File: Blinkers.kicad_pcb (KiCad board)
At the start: 2 copper layers, 238 x 45 mm, 218 parts, among them J1 12V, J2 A1, J3 gnd, J4 A1, J5 A1, J6 A1, J7 A1, J8 A1, Q1 Q_NMOS_DGS, Q2 Q_NMOS_DGS, Q3 Q_NMOS_DGS, Q4 Q_NMOS_DGS, Q5 Q_NMOS_DGS, Q6 Q_NMOS_DGS

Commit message: Edge-cuts have been set to the Nova layout.
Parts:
- moved R30 22.5 mm to (242.3, 90.7)
- moved R31 22.5 mm to (242.3, 105.2)
- moved D10 22.5 mm to (38.6, 100.1)
- moved D104 22.5 mm to (149.5, 94.5)
- moved D105 22.5 mm to (149.5, 100.1)
- moved D108 22.5 mm to (149.5, 116.8)
- moved D114 22.5 mm to (161.8, 94.5)
- moved D115 22.5 mm to (161.8, 100.1)
- moved D118 22.5 mm to (161.8, 116.8)
- moved D122 22.5 mm to (174.1, 94.5)
- moved D123 22.5 mm to (174.1, 100.1)
- moved D126 22.5 mm to (174.1, 116.8)
- moved D13 22.5 mm to (38.6, 116.8)
- moved D131 22.5 mm to (186.4, 94.5)
- moved D132 22.5 mm to (186.4, 100.1)
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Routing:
- net 12V: track 673.9 -> 0.00 mm
- net GND: track 609.1 -> 0.00 mm
- net Net-(D1-Pad1): track 81.5 -> 0.00 mm
- net Net-(D10-Pad1): track 70.3 -> 0.00 mm
- net Net-(D36-Pad1): track 51.6 -> 0.00 mm
- net Net-(D105-Pad1): track 51.4 -> 0.00 mm
- net Net-(D63-Pad1): track 42.0 -> 0.00 mm
- net Net-(D123-Pad1): track 41.5 -> 0.00 mm
- net Net-(D150-Pad1): track 41.5 -> 0.00 mm
- net Net-(D25-Pad2): track 17.7 -> 0.00 mm
- net Net-(D22-Pad2): track 13.6 -> 0.00 mm
- net Net-(D91-Pad2): track 12.5 -> 0.00 mm
- net Net-(D78-Pad1): track 10.0 -> 0.00 mm
- net Net-(D77-Pad1): track 10.0 -> 0.00 mm
- net Net-(D165-Pad1): track 10.0 -> 0.00 mm
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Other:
- board size 238 x 45 mm -> 250 x 49 mm

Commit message: Main array x-axis positions and top row x-axis positions close to finished, WIP.
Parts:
- removed D10, D103, D104, D105, D106, D107, D108, D11, D113, D114, D115, D116, D117, D118, D12, D121, D122, D123, D124, D125, D126, D13, D130, D131, D132, D133, D134, D135, D140, D141, D142, D143, D144, D145, D148, D149, D15, D150, D151, D152, D153, D157, D158, D159, D16, D160, D161, D162, D167, D168, D169, D17, D170, D171, D172, D18, D19, D2, D20, D3, D34, D35, D36, D37, D38, D39, D4, D44, D45, D46, D47, D48, D49, D5, D54, D55, D56, D57, D58, D59, D6, D61, D62, D63, D64, D65, D66, D70, D71, D72, D73, D74, D75, D8, D80, D81, D82, D83, D84, D85, D9, D94, D95, D96, D97, D98, D99: LED, Footprints:D_2835
- removed J2, J4, J7, J8: A1, Socket_Strips:Socket_Strip_Straight_1x01_Pitch2.54mm
- added D1: LED, Footprints:D_2835, F.Cu at (247.4, 121.3)
- added D1: LED, Footprints:D_2835, F.Cu at (132.6, 121.3)
- added D1: LED, Footprints:D_2835, F.Cu at (132.6, 95.4)
- added D1: LED, Footprints:D_2835, F.Cu at (119.8, 95.4)
- added D1: LED, Footprints:D_2835, F.Cu at (107.1, 95.4)
- added D1: LED, Footprints:D_2835, F.Cu at (94.3, 95.4)
- added D1: LED, Footprints:D_2835, F.Cu at (81.6, 95.4)
- added D1: LED, Footprints:D_2835, F.Cu at (68.8, 95.4)
- added D1: LED, Footprints:D_2835, F.Cu at (56.1, 95.4)
- added D1: LED, Footprints:D_2835, F.Cu at (43.3, 95.4)
- added D1: LED, Footprints:D_2835, F.Cu at (30.5, 95.4)
- added D1: LED, Footprints:D_2835, F.Cu at (247.4, 90.3)
- added D1: LED, Footprints:D_2835, F.Cu at (119.8, 121.3)
- added D1: LED, Footprints:D_2835, F.Cu at (234.6, 90.3)
- added D1: LED, Footprints:D_2835, F.Cu at (221.9, 90.3)
- added D1: LED, Footprints:D_2835, F.Cu at (209.1, 90.3)
- added D1: LED, Footprints:D_2835, F.Cu at (196.4, 90.3)
- added D1: LED, Footprints:D_2835, F.Cu at (183.6, 90.3)
- added D1: LED, Footprints:D_2835, F.Cu at (170.9, 90.3)
- added D1: LED, Footprints:D_2835, F.Cu at (158.1, 90.3)
- added D1: LED, Footprints:D_2835, F.Cu at (145.3, 90.3)
- added D1: LED, Footprints:D_2835, F.Cu at (132.6, 90.3)
- added D1: LED, Footprints:D_2835, F.Cu at (119.8, 90.3)
- added D1: LED, Footprints:D_2835, F.Cu at (107.1, 121.3)
- added D1: LED, Footprints:D_2835, F.Cu at (107.1, 90.3)
- added D1: LED, Footprints:D_2835, F.Cu at (94.3, 90.3)
- added D1: LED, Footprints:D_2835, F.Cu at (81.6, 90.3)
- added D1: LED, Footprints:D_2835, F.Cu at (68.8, 90.3)
- added D1: LED, Footprints:D_2835, F.Cu at (56.1, 90.3)
- added D1: LED, Footprints:D_2835, F.Cu at (43.3, 90.3)
- added D1: LED, Footprints:D_2835, F.Cu at (94.3, 121.3)
- added D1: LED, Footprints:D_2835, F.Cu at (81.6, 121.3)
- added D1: LED, Footprints:D_2835, F.Cu at (68.8, 121.3)
- added D1: LED, Footprints:D_2835, F.Cu at (56.1, 121.3)
- added D1: LED, Footprints:D_2835, F.Cu at (43.3, 121.3)
- added D1: LED, Footprints:D_2835, F.Cu at (30.5, 121.3)
- added D1: LED, Footprints:D_2835, F.Cu at (247.4, 116.1)
- added D1: LED, Footprints:D_2835, F.Cu at (234.6, 121.3)
- added D1: LED, Footprints:D_2835, F.Cu at (234.6, 116.1)
- added D1: LED, Footprints:D_2835, F.Cu at (221.9, 116.1)
- added D1: LED, Footprints:D_2835, F.Cu at (209.1, 116.1)
- added D1: LED, Footprints:D_2835, F.Cu at (196.4, 116.1)
- added D1: LED, Footprints:D_2835, F.Cu at (183.6, 116.1)
- added D1: LED, Footprints:D_2835, F.Cu at (170.9, 116.1)
- added D1: LED, Footprints:D_2835, F.Cu at (158.1, 116.1)
- added D1: LED, Footprints:D_2835, F.Cu at (145.3, 116.1)
- added D1: LED, Footprints:D_2835, F.Cu at (132.6, 116.1)
- added D1: LED, Footprints:D_2835, F.Cu at (119.8, 116.1)
- added D1: LED, Footprints:D_2835, F.Cu at (221.9, 121.3)
- added D1: LED, Footprints:D_2835, F.Cu at (107.1, 116.1)
- added D1: LED, Footprints:D_2835, F.Cu at (94.3, 116.1)
- added D1: LED, Footprints:D_2835, F.Cu at (81.6, 116.1)
- added D1: LED, Footprints:D_2835, F.Cu at (68.8, 116.1)
- added D1: LED, Footprints:D_2835, F.Cu at (56.1, 116.1)
- added D1: LED, Footprints:D_2835, F.Cu at (43.3, 116.1)
- added D1: LED, Footprints:D_2835, F.Cu at (30.5, 116.1)
- added D1: LED, Footprints:D_2835, F.Cu at (247.4, 111.0)
- added D1: LED, Footprints:D_2835, F.Cu at (234.6, 111.0)
- added D1: LED, Footprints:D_2835, F.Cu at (221.9, 111.0)
- added D1: LED, Footprints:D_2835, F.Cu at (209.1, 121.3)
- added D1: LED, Footprints:D_2835, F.Cu at (209.1, 111.0)
- added D1: LED, Footprints:D_2835, F.Cu at (196.4, 111.0)
- added D1: LED, Footprints:D_2835, F.Cu at (183.6, 111.0)
- added D1: LED, Footprints:D_2835, F.Cu at (170.9, 111.0)
- added D1: LED, Footprints:D_2835, F.Cu at (158.1, 111.0)
- added D1: LED, Footprints:D_2835, F.Cu at (145.3, 111.0)
- added D1: LED, Footprints:D_2835, F.Cu at (132.6, 111.0)
- added D1: LED, Footprints:D_2835, F.Cu at (119.8, 111.0)
- added D1: LED, Footprints:D_2835, F.Cu at (107.1, 111.0)
- added D1: LED, Footprints:D_2835, F.Cu at (94.3, 111.0)
- added D1: LED, Footprints:D_2835, F.Cu at (196.4, 121.3)
- added D1: LED, Footprints:D_2835, F.Cu at (81.6, 111.0)
- added D1: LED, Footprints:D_2835, F.Cu at (68.8, 111.0)
- added D1: LED, Footprints:D_2835, F.Cu at (56.1, 111.0)
- added D1: LED, Footprints:D_2835, F.Cu at (43.3, 111.0)
- added D1: LED, Footprints:D_2835, F.Cu at (30.5, 111.0)
- added D1: LED, Footprints:D_2835, F.Cu at (247.4, 105.8)
- added D1: LED, Footprints:D_2835, F.Cu at (234.6, 105.8)
- added D1: LED, Footprints:D_2835, F.Cu at (221.9, 105.8)
- added D1: LED, Footprints:D_2835, F.Cu at (209.1, 105.8)
- added D1: LED, Footprints:D_2835, F.Cu at (196.4, 105.8)
- added D1: LED, Footprints:D_2835, F.Cu at (183.6, 121.3)
- added D1: LED, Footprints:D_2835, F.Cu at (183.6, 105.8)
- added D1: LED, Footprints:D_2835, F.Cu at (170.9, 105.8)
- added D1: LED, Footprints:D_2835, F.Cu at (158.1, 105.8)
- added D1: LED, Footprints:D_2835, F.Cu at (145.3, 105.8)
- added D1: LED, Footprints:D_2835, F.Cu at (132.6, 105.8)
- added D1: LED, Footprints:D_2835, F.Cu at (119.8, 105.8)
- added D1: LED, Footprints:D_2835, F.Cu at (107.1, 105.8)
- added D1: LED, Footprints:D_2835, F.Cu at (94.3, 105.8)
- added D1: LED, Footprints:D_2835, F.Cu at (81.6, 105.8)
- added D1: LED, Footprints:D_2835, F.Cu at (68.8, 105.8)
- added D1: LED, Footprints:D_2835, F.Cu at (170.9, 121.3)
- added D1: LED, Footprints:D_2835, F.Cu at (56.1, 105.8)
- added D1: LED, Footprints:D_2835, F.Cu at (43.3, 105.8)
- added D1: LED, Footprints:D_2835, F.Cu at (30.5, 105.8)
- added D1: LED, Footprints:D_2835, F.Cu at (247.4, 100.6)
- added D1: LED, Footprints:D_2835, F.Cu at (234.6, 100.6)
- added D1: LED, Footprints:D_2835, F.Cu at (221.9, 100.6)
- added D1: LED, Footprints:D_2835, F.Cu at (209.1, 100.6)
- added D1: LED, Footprints:D_2835, F.Cu at (196.4, 100.6)
- added D1: LED, Footprints:D_2835, F.Cu at (183.6, 100.6)
- added D1: LED, Footprints:D_2835, F.Cu at (170.9, 100.6)
- added D1: LED, Footprints:D_2835, F.Cu at (158.1, 121.3)
- added D1: LED, Footprints:D_2835, F.Cu at (158.1, 100.6)
- added D1: LED, Footprints:D_2835, F.Cu at (145.3, 100.6)
- added D1: LED, Footprints:D_2835, F.Cu at (132.6, 100.6)
- added D1: LED, Footprints:D_2835, F.Cu at (119.8, 100.6)
- added D1: LED, Footprints:D_2835, F.Cu at (107.1, 100.6)
- added D1: LED, Footprints:D_2835, F.Cu at (94.3, 100.6)
- added D1: LED, Footprints:D_2835, F.Cu at (81.6, 100.6)
- added D1: LED, Footprints:D_2835, F.Cu at (68.8, 100.6)
- added D1: LED, Footprints:D_2835, F.Cu at (56.1, 100.6)
- added D1: LED, Footprints:D_2835, F.Cu at (43.3, 100.6)
- added D1: LED, Footprints:D_2835, F.Cu at (145.3, 121.3)
- added D1: LED, Footprints:D_2835, F.Cu at (30.5, 100.6)
- added D1: LED, Footprints:D_2835, F.Cu at (247.4, 95.4)
- added D1: LED, Footprints:D_2835, F.Cu at (234.6, 95.4)
- added D1: LED, Footprints:D_2835, F.Cu at (221.9, 95.4)
- added D1: LED, Footprints:D_2835, F.Cu at (209.1, 95.4)
- added D1: LED, Footprints:D_2835, F.Cu at (196.4, 95.4)
- added D1: LED, Footprints:D_2835, F.Cu at (183.6, 95.4)
- added D1: LED, Footprints:D_2835, F.Cu at (170.9, 95.4)
- added D1: LED, Footprints:D_2835, F.Cu at (158.1, 95.4)
- added D1: LED, Footprints:D_2835, F.Cu at (145.3, 95.4)
- moved R53 13.1 mm to (217.2, 80.0)
- moved D166 11.7 mm to (247.4, 85.1)
- moved D164 11.2 mm to (234.6, 85.1)
- moved D155 10.8 mm to (221.9, 85.1)
- moved R44 10.4 mm to (177.8, 81.3)
- moved D139 10.4 mm to (209.1, 85.1)
- moved D137 9.94 mm to (196.4, 85.1)
- moved D128 9.50 mm to (183.6, 85.1)
- moved R35 9.32 mm to (139.7, 81.3)
- moved D112 9.06 mm to (170.9, 85.1)
- moved D110 8.63 mm to (158.1, 85.1)
- moved D101 8.19 mm to (145.3, 85.1)
- moved R24 7.77 mm to (101.8, 83.8)
- moved D79 7.76 mm to (132.6, 85.1)
- moved D77 7.32 mm to (119.8, 85.1)
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
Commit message: Bottom and right columns aligned.
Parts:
- removed R14, R15, R17, R18, R19, R2, R20, R22, R23, R26, R27, R28, R29, R3, R33, R34, R37, R38, R39, R4, R40, R42, R43, R46, R47, R48, R49, R5, R51, R52, R55, R56, R57, R58, R6, R7: 145, Footprints:R_1206_EDIT
- removed R30, R31: R, Footprints:R_1206_EDIT
- moved Q6 14.2 mm to (252.7, 116.8)
- moved Q5 13.1 mm to (214.6, 116.8)
- moved R54 12.3 mm to (217.2, 127.0)
- moved Q4 12.0 mm to (176.5, 116.8)
- moved D174 11.7 mm to (247.4, 126.5)
- moved D165 11.2 mm to (234.6, 126.5)
- moved Q3 10.9 mm to (138.4, 116.8)
- moved D156 10.8 mm to (221.9, 126.5)
- moved D147 10.4 mm to (209.1, 126.5)
- moved Q2 10.1 mm to (100.3, 117.1)
- moved D138 9.93 mm to (196.4, 126.5)
- moved Q1 9.92 mm to (62.2, 118.1)
- moved R45 9.66 mm to (177.6, 127.0)
- moved D129 9.49 mm to (183.6, 126.5)
- moved D120 9.05 mm to (170.9, 126.5)
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
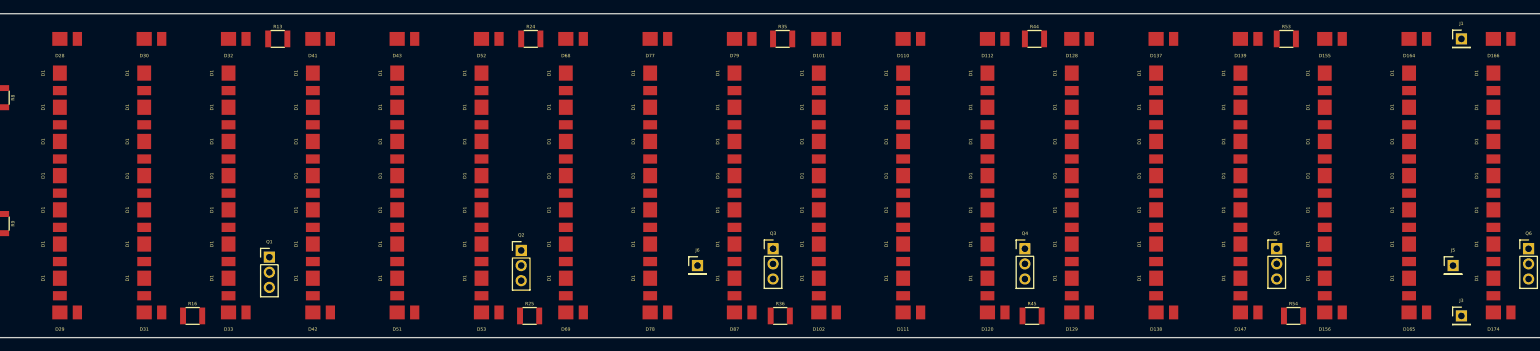
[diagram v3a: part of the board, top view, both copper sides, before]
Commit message: Columns and rows aligned. Outer ring aligned. Component designators assigned. VCC and GND positioned. Need to add remaining resistors and position transistors and their inputs.
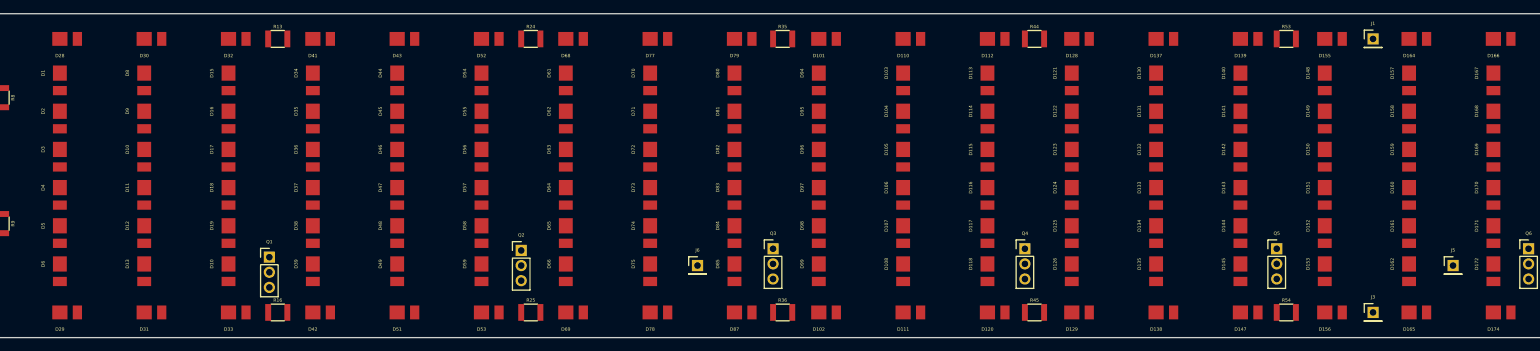
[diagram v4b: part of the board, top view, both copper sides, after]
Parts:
- removed the D1 at (247.4, 121.3)
- removed the D1 at (132.6, 121.3)
- removed the D1 at (119.8, 121.3)
- removed the D1 at (107.1, 121.3)
- removed the D1 at (94.3, 121.3)
- removed the D1 at (81.6, 121.3)
- removed the D1 at (68.8, 121.3)
- removed the D1 at (56.1, 121.3)
- removed the D1 at (43.3, 121.3)
- removed the D1 at (30.5, 121.3)
- removed the D1 at (247.4, 116.1)
- removed the D1 at (234.6, 121.3)
- removed the D1 at (234.6, 116.1)
- removed the D1 at (221.9, 116.1)
- removed the D1 at (209.1, 116.1)
- removed the D1 at (196.4, 116.1)
- removed the D1 at (183.6, 116.1)
- removed the D1 at (170.9, 116.1)
- removed the D1 at (158.1, 116.1)
- removed the D1 at (145.3, 116.1)
- removed the D1 at (132.6, 116.1)
- removed the D1 at (119.8, 116.1)
- removed the D1 at (221.9, 121.3)
- removed the D1 at (107.1, 116.1)
- removed the D1 at (94.3, 116.1)
- removed the D1 at (81.6, 116.1)
- removed the D1 at (68.8, 116.1)
- removed the D1 at (56.1, 116.1)
- removed the D1 at (43.3, 116.1)
- removed the D1 at (209.1, 121.3)
- removed the D1 at (196.4, 121.3)
- removed the D1 at (183.6, 121.3)
- removed the D1 at (170.9, 121.3)
- removed the D1 at (158.1, 121.3)
- removed the D1 at (145.3, 121.3)
- added D10: LED, Footprints:D_2835, F.Cu at (56.1, 119.1)
- added D108: LED, Footprints:D_2835, F.Cu at (158.1, 119.1)
- added D118: LED, Footprints:D_2835, F.Cu at (170.9, 119.1)
- added D126: LED, Footprints:D_2835, F.Cu at (183.6, 119.1)
- added D13: LED, Footprints:D_2835, F.Cu at (43.3, 119.1)
- added D135: LED, Footprints:D_2835, F.Cu at (196.4, 119.1)
- added D145: LED, Footprints:D_2835, F.Cu at (209.1, 119.1)
- added D153: LED, Footprints:D_2835, F.Cu at (221.9, 119.1)
- added D162: LED, Footprints:D_2835, F.Cu at (234.6, 119.1)
- added D172: LED, Footprints:D_2835, F.Cu at (247.4, 119.1)
- added D39: LED, Footprints:D_2835, F.Cu at (68.8, 119.1)
- added D49: LED, Footprints:D_2835, F.Cu at (81.6, 119.1)
- added D59: LED, Footprints:D_2835, F.Cu at (94.3, 119.1)
- added D66: LED, Footprints:D_2835, F.Cu at (107.1, 119.1)
- added D75: LED, Footprints:D_2835, F.Cu at (119.8, 119.1)
- added D85: LED, Footprints:D_2835, F.Cu at (132.6, 119.1)
- added D99: LED, Footprints:D_2835, F.Cu at (145.3, 119.1)
- moved J3 13.4 mm to (229.2, 126.5)
- moved J1 13.4 mm to (229.2, 85.1)
- moved R16 12.9 mm to (63.5, 126.5)
- moved D6 3.01 mm to (30.5, 119.1)
- moved D107 2.41 mm to (158.1, 113.4)
- moved D117 2.41 mm to (170.9, 113.4)
- moved D12 2.41 mm to (43.3, 113.4)
- moved D125 2.41 mm to (183.6, 113.4)
- moved D134 2.41 mm to (196.4, 113.4)
- moved D144 2.41 mm to (209.1, 113.4)
- moved D152 2.41 mm to (221.9, 113.4)
- moved D161 2.41 mm to (234.6, 113.4)
- moved D171 2.41 mm to (247.4, 113.4)
- moved D19 2.41 mm to (56.1, 113.4)
- moved D38 2.41 mm to (68.8, 113.4)
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- renumbered D1 to D10, D1 to D103, D1 to D104, D1 to D105, D1 to D106, D1 to D107, D1 to D11, D1 to D113, D1 to D114, D1 to D115, D1 to D116, D1 to D117, D1 to D12, D1 to D121, D1 to D122, D1 to D123, D1 to D124, D1 to D125, D1 to D130, D1 to D131, D1 to D132, D1 to D133, D1 to D134, D1 to D140, D1 to D141, D1 to D142, D1 to D143, D1 to D144, D1 to D148, D1 to D149, D1 to D15, D1 to D150, D1 to D151, D1 to D152, D1 to D157, D1 to D158, D1 to D159, D1 to D16, D1 to D160, D1 to D161, D1 to D167, D1 to D168, D1 to D169, D1 to D17, D1 to D170, D1 to D171, D1 to D18, D1 to D19, D1 to D2, D1 to D3, D1 to D34, D1 to D35, D1 to D36, D1 to D37, D1 to D38, D1 to D4, D1 to D44, D1 to D45, D1 to D46, D1 to D47, D1 to D48, D1 to D5, D1 to D54, D1 to D55, D1 to D56, D1 to D57, D1 to D58, D1 to D6, D1 to D61, D1 to D62, D1 to D63, D1 to D64, D1 to D65, D1 to D70, D1 to D71, D1 to D72, D1 to D73, D1 to D74, D1 to D8, D1 to D80, D1 to D81, D1 to D82, D1 to D83, D1 to D84, D1 to D9, D1 to D94, D1 to D95, D1 to D96, D1 to D97, D1 to D98

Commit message: Layout complete, ready for tracerouting.
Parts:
- added J2: A1, Socket_Strips:Socket_Strip_Straight_1x01_Pitch2.54mm, F.Cu at (228.6, 95.2)
- added J4: A1, Socket_Strips:Socket_Strip_Straight_1x01_Pitch2.54mm, F.Cu at (228.6, 99.1)
- added J7: A1, Socket_Strips:Socket_Strip_Straight_1x01_Pitch2.54mm, F.Cu at (228.6, 112.3)
- added J8: A1, Socket_Strips:Socket_Strip_Straight_1x01_Pitch2.54mm, F.Cu at (228.6, 116.1)
- added J9: brake, Socket_Strips:Socket_Strip_Straight_1x01_Pitch2.54mm, F.Cu at (241.3, 95.2)
- added R14: 145, Resistors_SMD:R_1206, F.Cu at (62.2, 90.3)
- added R15: 145, Resistors_SMD:R_1206, F.Cu at (62.2, 107.6)
- added R17: 145, Resistors_SMD:R_1206, F.Cu at (74.9, 90.3)
- added R18: 145, Resistors_SMD:R_1206, F.Cu at (74.9, 107.6)
- added R19: 145, Resistors_SMD:R_1206, F.Cu at (87.6, 90.3)
- added R2: 145, Resistors_SMD:R_1206, F.Cu at (24.1, 90.3)
- added R20: 145, Resistors_SMD:R_1206, F.Cu at (87.6, 107.6)
- added R22: 145, Resistors_SMD:R_1206, F.Cu at (100.3, 90.3)
- added R23: 145, Resistors_SMD:R_1206, F.Cu at (100.3, 107.6)
- added R26: 145, Resistors_SMD:R_1206, F.Cu at (113.0, 90.3)
- added R27: 145, Resistors_SMD:R_1206, F.Cu at (113.0, 107.6)
- added R28: 145, Resistors_SMD:R_1206, F.Cu at (125.7, 90.3)
- added R29: 145, Resistors_SMD:R_1206, F.Cu at (125.7, 107.6)
- added R3: 145, Resistors_SMD:R_1206, F.Cu at (24.1, 107.6)
- added R30: R, Resistors_SMD:R_1206, F.Cu at (252.7, 90.2)
- added R31: R, Resistors_SMD:R_1206, F.Cu at (252.7, 108.0)
- added R33: 145, Resistors_SMD:R_1206, F.Cu at (138.4, 90.3)
- added R34: 145, Resistors_SMD:R_1206, F.Cu at (138.4, 107.6)
- added R37: 145, Resistors_SMD:R_1206, F.Cu at (151.1, 90.3)
- added R38: 145, Resistors_SMD:R_1206, F.Cu at (151.1, 107.6)
- added R39: 145, Resistors_SMD:R_1206, F.Cu at (163.8, 90.3)
- added R4: 145, Resistors_SMD:R_1206, F.Cu at (36.8, 90.3)
- added R40: 145, Resistors_SMD:R_1206, F.Cu at (163.8, 107.6)
- added R42: 145, Resistors_SMD:R_1206, F.Cu at (176.5, 90.3)
- added R43: 145, Resistors_SMD:R_1206, F.Cu at (176.7, 107.6)
- added R46: 145, Resistors_SMD:R_1206, F.Cu at (189.2, 90.3)
- added R47: 145, Resistors_SMD:R_1206, F.Cu at (189.2, 107.6)
- added R48: 145, Resistors_SMD:R_1206, F.Cu at (203.2, 90.3)
- added R49: 145, Resistors_SMD:R_1206, F.Cu at (201.9, 107.6)
- added R5: 145, Resistors_SMD:R_1206, F.Cu at (36.8, 107.6)
- added R51: 145, Resistors_SMD:R_1206, F.Cu at (215.9, 90.3)
- added R52: 145, Resistors_SMD:R_1206, F.Cu at (215.9, 107.6)
- added R55: 145, Resistors_SMD:R_1206, F.Cu at (228.6, 90.3)
- added R56: 145, Resistors_SMD:R_1206, F.Cu at (228.6, 107.6)
- added R57: 145, Resistors_SMD:R_1206, F.Cu at (241.3, 90.3)
- added R58: 145, Resistors_SMD:R_1206, F.Cu at (241.3, 107.6)
- added R6: 145, Resistors_SMD:R_1206, F.Cu at (49.5, 90.3)
- added R7: 145, Resistors_SMD:R_1206, F.Cu at (49.5, 107.6)
- moved J6 102.9 mm to (228.6, 102.9), turned to 90 degrees
- moved J5 12.7 mm to (228.6, 119.9), turned to 90 degrees
- moved Q1 4.75 mm to (62.2, 113.4)
- moved Q2 3.73 mm to (100.3, 113.4)
- moved Q5 3.70 mm to (215.9, 113.4)
- moved Q4 3.48 mm to (176.7, 113.4)
- moved Q3 3.48 mm to (138.4, 113.4)
- moved Q6 3.48 mm to (252.7, 113.4)
- moved R8 3.27 mm to (24.1, 96.0), turned to 180 degrees
- moved R9 2.56 mm to (24.1, 113.4), turned to 180 degrees
- renumbered D10 to D20
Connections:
- D10 pad 1: Net-(D1-Pad1) -> Net-(D10-Pad1)
- D10 pad 2: Net-(D1-Pad2) -> Net-(D10-Pad2)
- D103 pad 1: Net-(D1-Pad1) -> Net-(D103-Pad1)
- D103 pad 2: Net-(D1-Pad2) -> Net-(D103-Pad2)
- D104 pad 1: Net-(D1-Pad1) -> Net-(D104-Pad1)
- D104 pad 2: Net-(D1-Pad2) -> Net-(D103-Pad1)
- D105 pad 1: Net-(D1-Pad1) -> Net-(D105-Pad1)
- D105 pad 2: Net-(D1-Pad2) -> Net-(D104-Pad1)
- D106 pad 1: Net-(D1-Pad1) -> Net-(D106-Pad1)
- D106 pad 2: Net-(D1-Pad2) -> Net-(D106-Pad2)
- D107 pad 1: Net-(D1-Pad1) -> Net-(D107-Pad1)
- D107 pad 2: Net-(D1-Pad2) -> Net-(D106-Pad1)
- D108 pad 1: Net-(D1-Pad1) -> Net-(D105-Pad1)
- D108 pad 2: Net-(D1-Pad2) -> Net-(D107-Pad1)
- D11 pad 1: Net-(D1-Pad1) -> Net-(D11-Pad1)
- D11 pad 2: Net-(D1-Pad2) -> Net-(D11-Pad2)
- D113 pad 1: Net-(D1-Pad1) -> Net-(D113-Pad1)
- D113 pad 2: Net-(D1-Pad2) -> Net-(D113-Pad2)
- D114 pad 1: Net-(D1-Pad1) -> Net-(D114-Pad1)
- D114 pad 2: Net-(D1-Pad2) -> Net-(D113-Pad1)
- D115 pad 1: Net-(D1-Pad1) -> Net-(D105-Pad1)
- D115 pad 2: Net-(D1-Pad2) -> Net-(D114-Pad1)
- D116 pad 1: Net-(D1-Pad1) -> Net-(D116-Pad1)
- D116 pad 2: Net-(D1-Pad2) -> Net-(D116-Pad2)
- D117 pad 1: Net-(D1-Pad1) -> Net-(D117-Pad1)
- D117 pad 2: Net-(D1-Pad2) -> Net-(D116-Pad1)
- D118 pad 1: Net-(D1-Pad1) -> Net-(D105-Pad1)
- D118 pad 2: Net-(D1-Pad2) -> Net-(D117-Pad1)
- D12 pad 1: Net-(D1-Pad1) -> Net-(D12-Pad1)
- D12 pad 2: Net-(D1-Pad2) -> Net-(D11-Pad1)
- D121 pad 1: Net-(D1-Pad1) -> Net-(D121-Pad1)
- D121 pad 2: Net-(D1-Pad2) -> Net-(D121-Pad2)
- D122 pad 1: Net-(D1-Pad1) -> Net-(D122-Pad1)
- D122 pad 2: Net-(D1-Pad2) -> Net-(D121-Pad1)
- D123 pad 1: Net-(D1-Pad1) -> Net-(D123-Pad1)
- D123 pad 2: Net-(D1-Pad2) -> Net-(D122-Pad1)
- D124 pad 1: Net-(D1-Pad1) -> Net-(D124-Pad1)
- D124 pad 2: Net-(D1-Pad2) -> Net-(D124-Pad2)
- D125 pad 1: Net-(D1-Pad1) -> Net-(D125-Pad1)
- D125 pad 2: Net-(D1-Pad2) -> Net-(D124-Pad1)
- D126 pad 1: Net-(D1-Pad1) -> Net-(D123-Pad1)
- D126 pad 2: Net-(D1-Pad2) -> Net-(D125-Pad1)
- D13 pad 1: Net-(D1-Pad1) -> Net-(D10-Pad1)
- D13 pad 2: Net-(D1-Pad2) -> Net-(D12-Pad1)
- D130 pad 1: Net-(D1-Pad1) -> Net-(D130-Pad1)
- D130 pad 2: Net-(D1-Pad2) -> Net-(D130-Pad2)
- D131 pad 1: Net-(D1-Pad1) -> Net-(D131-Pad1)
- D131 pad 2: Net-(D1-Pad2) -> Net-(D130-Pad1)
- D132 pad 1: Net-(D1-Pad1) -> Net-(D123-Pad1)
- D132 pad 2: Net-(D1-Pad2) -> Net-(D131-Pad1)
- D133 pad 1: Net-(D1-Pad1) -> Net-(D133-Pad1)
- D133 pad 2: Net-(D1-Pad2) -> Net-(D133-Pad2)
- D134 pad 1: Net-(D1-Pad1) -> Net-(D134-Pad1)
- D134 pad 2: Net-(D1-Pad2) -> Net-(D133-Pad1)
- D135 pad 1: Net-(D1-Pad1) -> Net-(D123-Pad1)
- D135 pad 2: Net-(D1-Pad2) -> Net-(D134-Pad1)
- D140 pad 1: Net-(D1-Pad1) -> Net-(D140-Pad1)
- D140 pad 2: Net-(D1-Pad2) -> Net-(D140-Pad2)
- D141 pad 1: Net-(D1-Pad1) -> Net-(D141-Pad1)
- D141 pad 2: Net-(D1-Pad2) -> Net-(D140-Pad1)
- D142 pad 1: Net-(D1-Pad1) -> Net-(D123-Pad1)
- D142 pad 2: Net-(D1-Pad2) -> Net-(D141-Pad1)
- D143 pad 1: Net-(D1-Pad1) -> Net-(D143-Pad1)
- D143 pad 2: Net-(D1-Pad2) -> Net-(D143-Pad2)
- D144 pad 1: Net-(D1-Pad1) -> Net-(D144-Pad1)
- D144 pad 2: Net-(D1-Pad2) -> Net-(D143-Pad1)
- D145 pad 1: Net-(D1-Pad1) -> Net-(D123-Pad1)
- D145 pad 2: Net-(D1-Pad2) -> Net-(D144-Pad1)
- D148 pad 1: Net-(D1-Pad1) -> Net-(D148-Pad1)
- D148 pad 2: Net-(D1-Pad2) -> Net-(D148-Pad2)
- D149 pad 1: Net-(D1-Pad1) -> Net-(D149-Pad1)
- D149 pad 2: Net-(D1-Pad2) -> Net-(D148-Pad1)
- D15 pad 1: Net-(D1-Pad1) -> Net-(D15-Pad1)
- D15 pad 2: Net-(D1-Pad2) -> Net-(D15-Pad2)
- D150 pad 1: Net-(D1-Pad1) -> Net-(D150-Pad1)
- D150 pad 2: Net-(D1-Pad2) -> Net-(D149-Pad1)
- D151 pad 1: Net-(D1-Pad1) -> Net-(D151-Pad1)
- D151 pad 2: Net-(D1-Pad2) -> Net-(D151-Pad2)
- D152 pad 1: Net-(D1-Pad1) -> Net-(D152-Pad1)
- D152 pad 2: Net-(D1-Pad2) -> Net-(D151-Pad1)
- D153 pad 1: Net-(D1-Pad1) -> Net-(D150-Pad1)
- D153 pad 2: Net-(D1-Pad2) -> Net-(D152-Pad1)
- D157 pad 1: Net-(D1-Pad1) -> Net-(D157-Pad1)
- D157 pad 2: Net-(D1-Pad2) -> Net-(D157-Pad2)
- D158 pad 1: Net-(D1-Pad1) -> Net-(D158-Pad1)
- D158 pad 2: Net-(D1-Pad2) -> Net-(D157-Pad1)
- D159 pad 1: Net-(D1-Pad1) -> Net-(D150-Pad1)
- D159 pad 2: Net-(D1-Pad2) -> Net-(D158-Pad1)
- D16 pad 1: Net-(D1-Pad1) -> Net-(D16-Pad1)
- D16 pad 2: Net-(D1-Pad2) -> Net-(D15-Pad1)
- D160 pad 1: Net-(D1-Pad1) -> Net-(D160-Pad1)
- D160 pad 2: Net-(D1-Pad2) -> Net-(D160-Pad2)
- D161 pad 1: Net-(D1-Pad1) -> Net-(D161-Pad1)
- D161 pad 2: Net-(D1-Pad2) -> Net-(D160-Pad1)
- D162 pad 1: Net-(D1-Pad1) -> Net-(D150-Pad1)
- D162 pad 2: Net-(D1-Pad2) -> Net-(D161-Pad1)
- D167 pad 1: Net-(D1-Pad1) -> Net-(D167-Pad1)
- D167 pad 2: Net-(D1-Pad2) -> Net-(D167-Pad2)
- D168 pad 1: Net-(D1-Pad1) -> Net-(D168-Pad1)
- D168 pad 2: Net-(D1-Pad2) -> Net-(D167-Pad1)
- D169 pad 1: Net-(D1-Pad1) -> Net-(D150-Pad1)
- D169 pad 2: Net-(D1-Pad2) -> Net-(D168-Pad1)
- D17 pad 1: Net-(D1-Pad1) -> Net-(D10-Pad1)
- D17 pad 2: Net-(D1-Pad2) -> Net-(D16-Pad1)
- D170 pad 1: Net-(D1-Pad1) -> Net-(D170-Pad1)
- D170 pad 2: Net-(D1-Pad2) -> Net-(D170-Pad2)
- D171 pad 1: Net-(D1-Pad1) -> Net-(D171-Pad1)
- D171 pad 2: Net-(D1-Pad2) -> Net-(D170-Pad1)
- D172 pad 1: Net-(D1-Pad1) -> Net-(D150-Pad1)
- D172 pad 2: Net-(D1-Pad2) -> Net-(D171-Pad1)
- D18 pad 1: Net-(D1-Pad1) -> Net-(D18-Pad1)
- D18 pad 2: Net-(D1-Pad2) -> Net-(D18-Pad2)
- D19 pad 1: Net-(D1-Pad1) -> Net-(D19-Pad1)
- D19 pad 2: Net-(D1-Pad2) -> Net-(D18-Pad1)
- D2 pad 1: Net-(D1-Pad1) -> Net-(D2-Pad1)
- D2 pad 2: Net-(D1-Pad2) -> Net-(D1-Pad1)
- D20 pad 1: Net-(D1-Pad1) -> Net-(D10-Pad1)
- D20 pad 2: Net-(D1-Pad2) -> Net-(D19-Pad1)
- D3 pad 1: Net-(D1-Pad1) -> Net-(D10-Pad1)
- D3 pad 2: Net-(D1-Pad2) -> Net-(D2-Pad1)
- D34 pad 1: Net-(D1-Pad1) -> Net-(D34-Pad1)
- D34 pad 2: Net-(D1-Pad2) -> Net-(D34-Pad2)
- D35 pad 1: Net-(D1-Pad1) -> Net-(D35-Pad1)
- D35 pad 2: Net-(D1-Pad2) -> Net-(D34-Pad1)
- D36 pad 1: Net-(D1-Pad1) -> Net-(D36-Pad1)
- D36 pad 2: Net-(D1-Pad2) -> Net-(D35-Pad1)
- D37 pad 1: Net-(D1-Pad1) -> Net-(D37-Pad1)
- D37 pad 2: Net-(D1-Pad2) -> Net-(D37-Pad2)
- D38 pad 1: Net-(D1-Pad1) -> Net-(D38-Pad1)
- D38 pad 2: Net-(D1-Pad2) -> Net-(D37-Pad1)
- D39 pad 1: Net-(D1-Pad1) -> Net-(D36-Pad1)
- D39 pad 2: Net-(D1-Pad2) -> Net-(D38-Pad1)
- D4 pad 1: Net-(D1-Pad1) -> Net-(D4-Pad1)
- D4 pad 2: Net-(D1-Pad2) -> Net-(D4-Pad2)
- D44 pad 1: Net-(D1-Pad1) -> Net-(D44-Pad1)
- D44 pad 2: Net-(D1-Pad2) -> Net-(D44-Pad2)
- D45 pad 1: Net-(D1-Pad1) -> Net-(D45-Pad1)
- D45 pad 2: Net-(D1-Pad2) -> Net-(D44-Pad1)
- D46 pad 1: Net-(D1-Pad1) -> Net-(D36-Pad1)
- D46 pad 2: Net-(D1-Pad2) -> Net-(D45-Pad1)
- D47 pad 1: Net-(D1-Pad1) -> Net-(D47-Pad1)
- D47 pad 2: Net-(D1-Pad2) -> Net-(D47-Pad2)
- D48 pad 1: Net-(D1-Pad1) -> Net-(D48-Pad1)
- D48 pad 2: Net-(D1-Pad2) -> Net-(D47-Pad1)
- D49 pad 1: Net-(D1-Pad1) -> Net-(D36-Pad1)
- D49 pad 2: Net-(D1-Pad2) -> Net-(D48-Pad1)
- D5 pad 1: Net-(D1-Pad1) -> Net-(D5-Pad1)
- D5 pad 2: Net-(D1-Pad2) -> Net-(D4-Pad1)
- D54 pad 1: Net-(D1-Pad1) -> Net-(D54-Pad1)
- D54 pad 2: Net-(D1-Pad2) -> Net-(D54-Pad2)
- D55 pad 1: Net-(D1-Pad1) -> Net-(D55-Pad1)
- D55 pad 2: Net-(D1-Pad2) -> Net-(D54-Pad1)
- D56 pad 1: Net-(D1-Pad1) -> Net-(D36-Pad1)
- D56 pad 2: Net-(D1-Pad2) -> Net-(D55-Pad1)
- D57 pad 1: Net-(D1-Pad1) -> Net-(D57-Pad1)
- D57 pad 2: Net-(D1-Pad2) -> Net-(D57-Pad2)
- D58 pad 1: Net-(D1-Pad1) -> Net-(D58-Pad1)
- D58 pad 2: Net-(D1-Pad2) -> Net-(D57-Pad1)
- D59 pad 1: Net-(D1-Pad1) -> Net-(D36-Pad1)
- D59 pad 2: Net-(D1-Pad2) -> Net-(D58-Pad1)
- D6 pad 1: Net-(D1-Pad1) -> Net-(D10-Pad1)
- D6 pad 2: Net-(D1-Pad2) -> Net-(D5-Pad1)
- D61 pad 1: Net-(D1-Pad1) -> Net-(D61-Pad1)
- D61 pad 2: Net-(D1-Pad2) -> Net-(D61-Pad2)
- D62 pad 1: Net-(D1-Pad1) -> Net-(D62-Pad1)
- D62 pad 2: Net-(D1-Pad2) -> Net-(D61-Pad1)
- D63 pad 1: Net-(D1-Pad1) -> Net-(D63-Pad1)
- D63 pad 2: Net-(D1-Pad2) -> Net-(D62-Pad1)
- D64 pad 1: Net-(D1-Pad1) -> Net-(D64-Pad1)
- D64 pad 2: Net-(D1-Pad2) -> Net-(D64-Pad2)
- D65 pad 1: Net-(D1-Pad1) -> Net-(D65-Pad1)
- D65 pad 2: Net-(D1-Pad2) -> Net-(D64-Pad1)
- D66 pad 1: Net-(D1-Pad1) -> Net-(D63-Pad1)
- D66 pad 2: Net-(D1-Pad2) -> Net-(D65-Pad1)
- D70 pad 1: Net-(D1-Pad1) -> Net-(D70-Pad1)
- D70 pad 2: Net-(D1-Pad2) -> Net-(D70-Pad2)
- D71 pad 1: Net-(D1-Pad1) -> Net-(D71-Pad1)
- D71 pad 2: Net-(D1-Pad2) -> Net-(D70-Pad1)
- D72 pad 1: Net-(D1-Pad1) -> Net-(D63-Pad1)
- D72 pad 2: Net-(D1-Pad2) -> Net-(D71-Pad1)
- D73 pad 1: Net-(D1-Pad1) -> Net-(D73-Pad1)
- D73 pad 2: Net-(D1-Pad2) -> Net-(D73-Pad2)
- D74 pad 1: Net-(D1-Pad1) -> Net-(D74-Pad1)
- D74 pad 2: Net-(D1-Pad2) -> Net-(D73-Pad1)
- D75 pad 1: Net-(D1-Pad1) -> Net-(D63-Pad1)
- D75 pad 2: Net-(D1-Pad2) -> Net-(D74-Pad1)
- D8 pad 1: Net-(D1-Pad1) -> Net-(D8-Pad1)
- D8 pad 2: Net-(D1-Pad2) -> Net-(D8-Pad2)
- D80 pad 1: Net-(D1-Pad1) -> Net-(D80-Pad1)
- D80 pad 2: Net-(D1-Pad2) -> Net-(D80-Pad2)
- D81 pad 1: Net-(D1-Pad1) -> Net-(D81-Pad1)
- D81 pad 2: Net-(D1-Pad2) -> Net-(D80-Pad1)
- D82 pad 1: Net-(D1-Pad1) -> Net-(D63-Pad1)
- D82 pad 2: Net-(D1-Pad2) -> Net-(D81-Pad1)
- D83 pad 1: Net-(D1-Pad1) -> Net-(D83-Pad1)
- D83 pad 2: Net-(D1-Pad2) -> Net-(D83-Pad2)
- D84 pad 1: Net-(D1-Pad1) -> Net-(D84-Pad1)
- D84 pad 2: Net-(D1-Pad2) -> Net-(D83-Pad1)
- D85 pad 1: Net-(D1-Pad1) -> Net-(D63-Pad1)
- D85 pad 2: Net-(D1-Pad2) -> Net-(D84-Pad1)
- D9 pad 1: Net-(D1-Pad1) -> Net-(D10-Pad2)
- D9 pad 2: Net-(D1-Pad2) -> Net-(D8-Pad1)
- D94 pad 1: Net-(D1-Pad1) -> Net-(D94-Pad1)
- D94 pad 2: Net-(D1-Pad2) -> Net-(D94-Pad2)
- D95 pad 1: Net-(D1-Pad1) -> Net-(D95-Pad1)
- D95 pad 2: Net-(D1-Pad2) -> Net-(D94-Pad1)
- D96 pad 1: Net-(D1-Pad1) -> Net-(D105-Pad1)
- D96 pad 2: Net-(D1-Pad2) -> Net-(D95-Pad1)
- D97 pad 1: Net-(D1-Pad1) -> Net-(D97-Pad1)
- D97 pad 2: Net-(D1-Pad2) -> Net-(D97-Pad2)
- D98 pad 1: Net-(D1-Pad1) -> Net-(D98-Pad1)
- D98 pad 2: Net-(D1-Pad2) -> Net-(D97-Pad1)
- D99 pad 1: Net-(D1-Pad1) -> Net-(D105-Pad1)
- D99 pad 2: Net-(D1-Pad2) -> Net-(D98-Pad1)
- R10 pad 1: 12V -> Brake
- R11 pad 1: 12V -> Brake
- R13 pad 1: 12V -> Brake
- R16 pad 1: 12V -> Brake
- R24 pad 1: 12V -> Brake
- R25 pad 1: 12V -> Brake
- R35 pad 1: 12V -> Brake
- R36 pad 1: 12V -> Brake
- R44 pad 1: 12V -> Brake
- R45 pad 1: 12V -> Brake
- R53 pad 1: 12V -> Brake
- R54 pad 1: 12V -> Brake
- R8 pad 1: 12V -> Brake
- R9 pad 1: 12V -> Brake

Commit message: Nova Board v1 complete!
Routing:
- net GND: track 0.00 -> 577.8 mm, vias 0 -> 2
- net Brake: track 0.00 -> 528.8 mm
- net 12V: track 0.00 -> 493.1 mm, vias 0 -> 1
- net Net-(J2-Pad1): track 0.00 -> 174.8 mm
- net Net-(J4-Pad1): track 0.00 -> 135.1 mm
- net Net-(D10-Pad1): track 0.00 -> 95.6 mm
- net Net-(J6-Pad1): track 0.00 -> 95.5 mm
- net Net-(D150-Pad1): track 0.00 -> 92.4 mm
- net Net-(D123-Pad1): track 0.00 -> 91.9 mm
- net Net-(D36-Pad1): track 0.00 -> 91.9 mm
- net Net-(D105-Pad1): track 0.00 -> 89.4 mm
- net Net-(D63-Pad1): track 0.00 -> 88.3 mm
- net Net-(J7-Pad1): track 0.00 -> 53.4 mm
- net Net-(J5-Pad1): track 0.00 -> 25.9 mm
- net Net-(D165-Pad1): track 0.00 -> 19.3 mm
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
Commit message: Moved VCC and GND inputs.
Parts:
- moved J3 33.9 mm to (215.9, 95.2), turned to 90 degrees
- moved J1 22.2 mm to (215.9, 102.9), turned to 90 degrees
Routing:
- net GND: track 577.8 -> 0.00 mm, vias 2 -> 0
- net Brake: track 528.8 -> 0.00 mm
- net 12V: track 493.1 -> 0.00 mm, vias 1 -> 0
- net Net-(J2-Pad1): track 174.8 -> 0.00 mm
- net Net-(J4-Pad1): track 135.1 -> 0.00 mm
- net Net-(D10-Pad1): track 95.6 -> 0.00 mm
- net Net-(J6-Pad1): track 95.5 -> 0.00 mm
- net Net-(D150-Pad1): track 92.4 -> 0.00 mm
- net Net-(D123-Pad1): track 91.9 -> 0.00 mm
- net Net-(D36-Pad1): track 91.9 -> 0.00 mm
- net Net-(D105-Pad1): track 89.4 -> 0.00 mm
- net Net-(D63-Pad1): track 88.3 -> 0.00 mm
- net Net-(J7-Pad1): track 53.4 -> 0.00 mm
- net Net-(J5-Pad1): track 25.9 -> 0.00 mm
- net Net-(D165-Pad1): track 19.3 -> 0.00 mm
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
